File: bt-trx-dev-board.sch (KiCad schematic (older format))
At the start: 13 parts, among them J1 RJ45, J2 PTT_BUTTON, J3 PTT_CON, J5 PTT_SELECT, U1 SILabs_WT32i

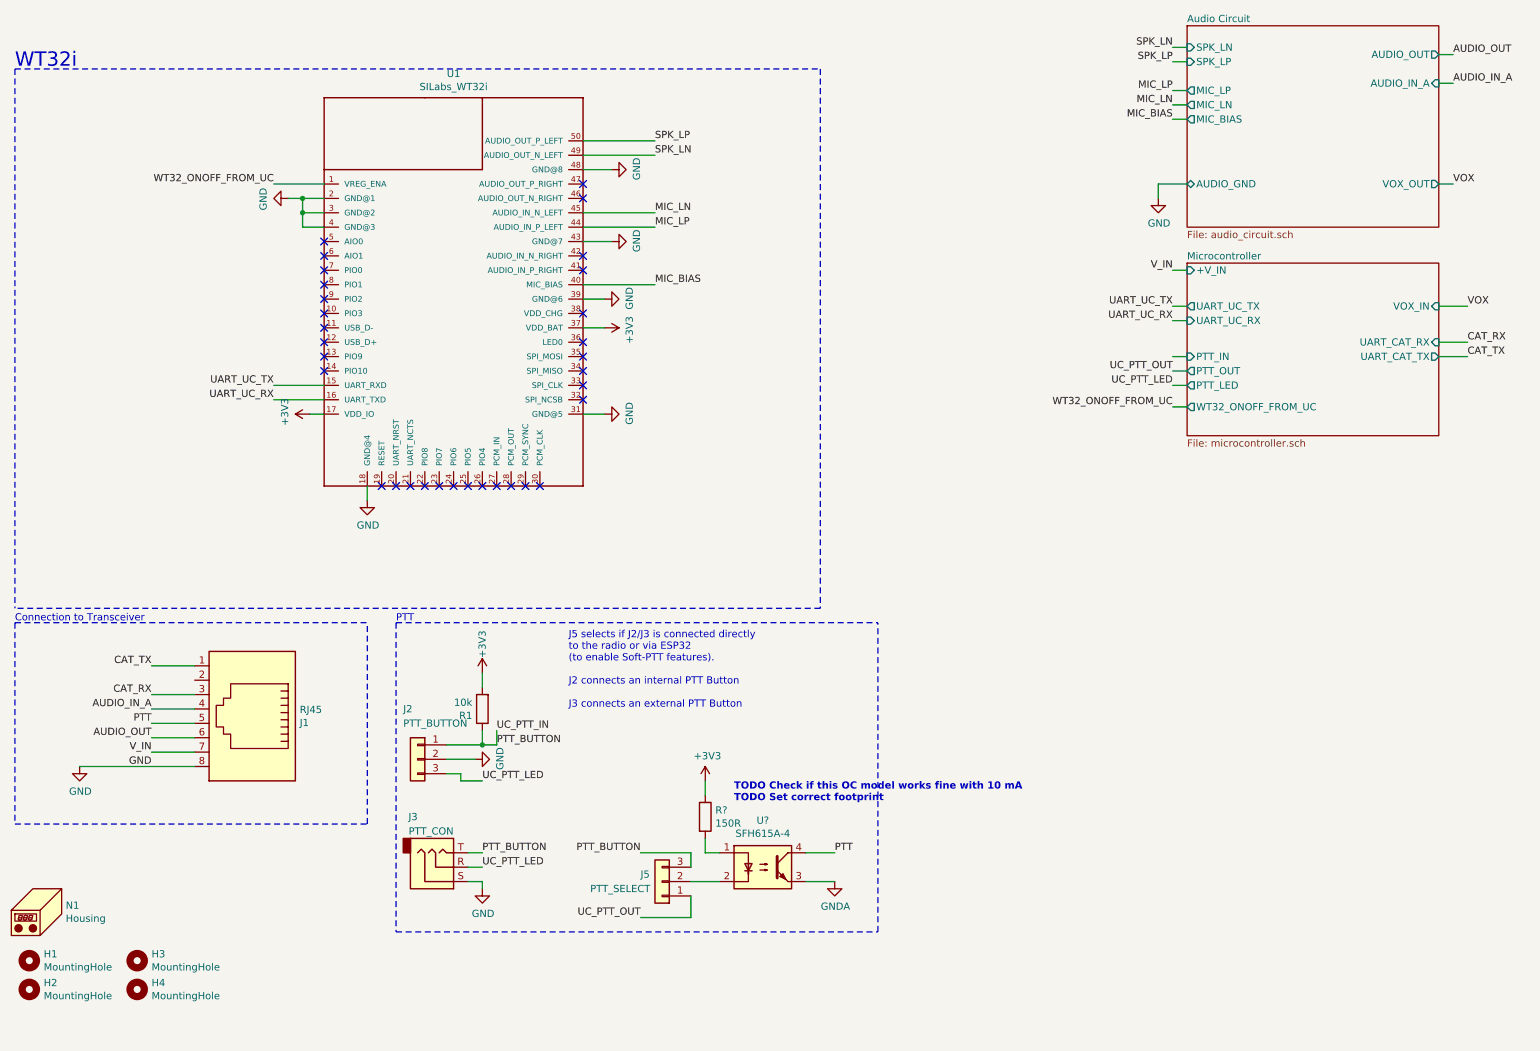
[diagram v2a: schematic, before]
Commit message: Audio Rework in Schematic [#21]
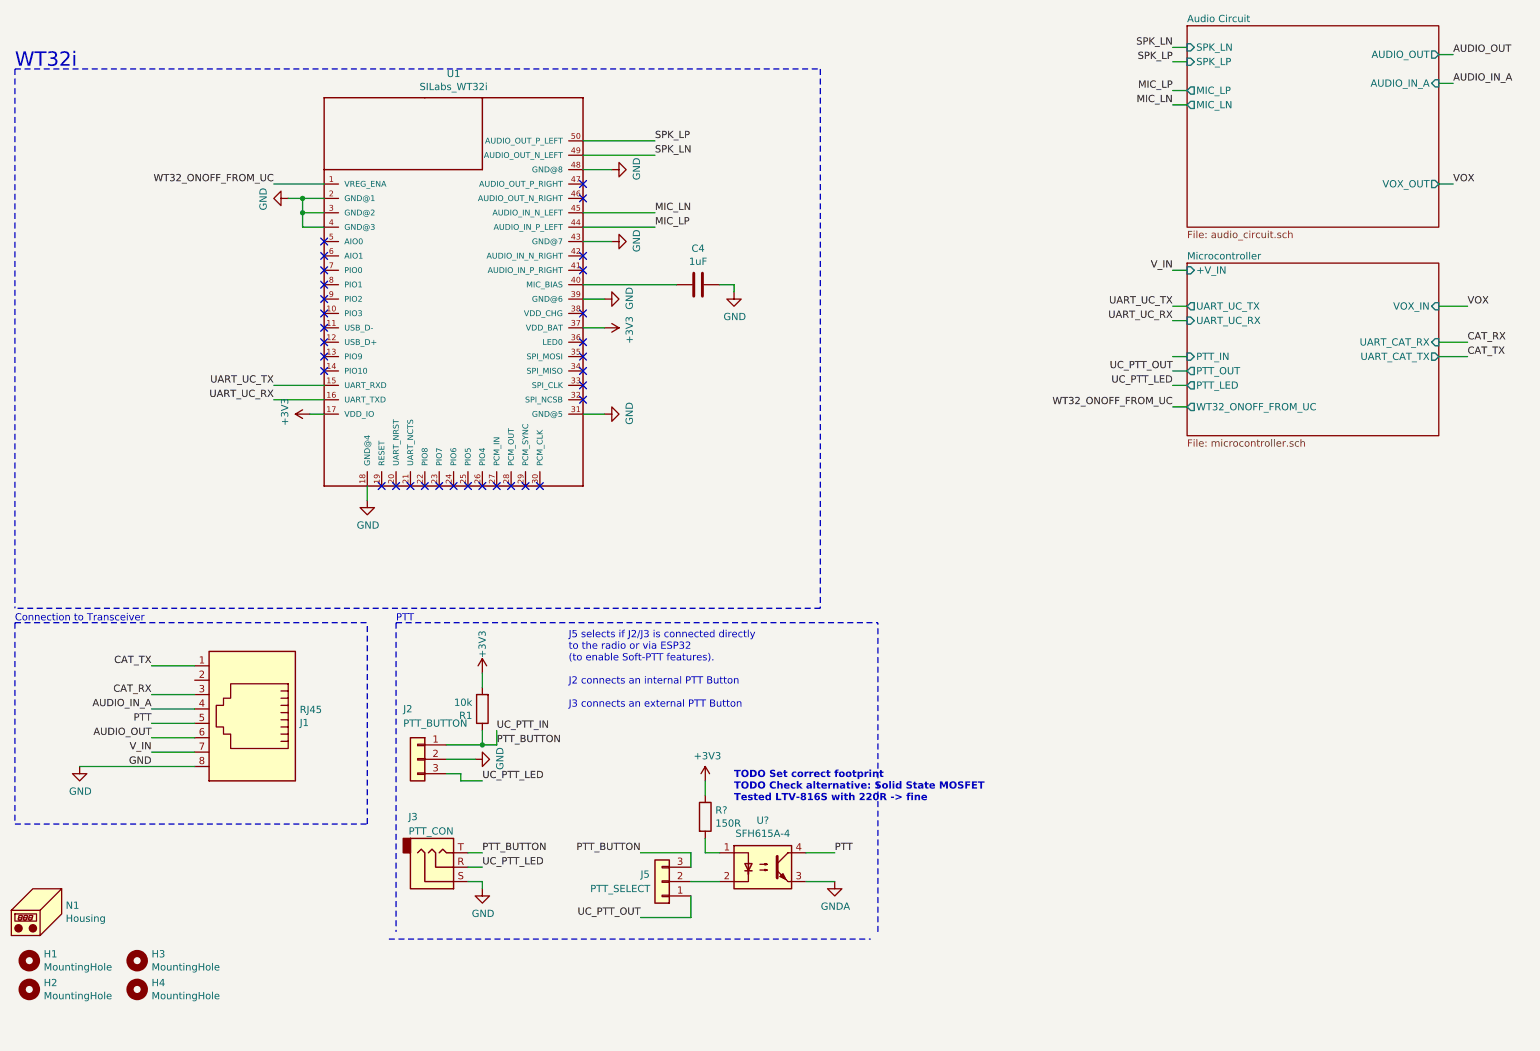
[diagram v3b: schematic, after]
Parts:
- added C4: 1uF, Capacitor_SMD:C_0805_2012Metric_Pad1.15x1.40mm_HandSolder, symbol Device:C
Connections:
- net GND: now also C4.1
- net MIC_BIAS: no longer names the net of U1.40 (MIC_BIAS)
- net MIC_BIAS: now also C4.2
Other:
- note added: "TODO Set correct footprint\nTODO Check alternative: Solid State MOSFET\nTested LTV-816S with 220R -> fine"
- note removed: "TODO Check if this OC model works fine with 10 mA\nTODO Set correct footprint"
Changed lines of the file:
@@
 EESchema Schematic File Version 4
-LIBS:bt-trx-dev-board-cache
 EELAYER 30 0
 EELAYER END
@@
 $EndComp
 NoConn ~ 4650 2650
-Text Label 5150 2450 0    50   ~ 0
-MIC_BIAS
-Wire Wire Line
-	8850 1300 8750 1300
-Text Label 8750 1300 2    50   ~ 0
-MIC_BIAS
 $Comp
 L power:+3V3 #PWR03
@@
 Wire Wire Line
 	4650 2050 5150 2050
-Wire Wire Line
-	4650 2450 5150 2450
 Text Label 2500 3250 2    50   ~ 0
 UART_UC_RX
@@
 F4 "AUDIO_OUT" O R 10600 850 50
 F5 "SPK_LN" I L 8850 800 50
-F6 "MIC_BIAS" O L 8850 1300 50
-F7 "AUDIO_IN_A" I R 10600 1050 50
-F8 "AUDIO_GND" B L 8850 1750 50
-F9 "SPK_LP" I L 8850 900 50
-F10 "VOX_OUT" O R 10600 1750 50
+F6 "AUDIO_IN_A" I R 10600 1050 50
+F7 "SPK_LP" I L 8850 900 50
+F8 "VOX_OUT" O R 10600 1750 50
 $EndSheet
 Wire Wire Line
@@
 Wire Wire Line
 	8850 800  8750 800
-$Comp
-L power:GND #PWR013
-U 1 1 5C781CAB
-P 8650 1850
-F 0 "#PWR013" H 8650 1600 50  0001 C CNN
-F 1 "GND" H 8655 1677 50  0000 C CNN
-F 2 "" H 8650 1850 50  0001 C CNN
-F 3 "" H 8650 1850 50  0001 C CNN
-	1    8650 1850
-	1    0    0    -1
-$EndComp
-Wire Wire Line
-	8850 1750 8650 1750
-Wire Wire Line
-	8650 1750 8650 1850
 $Comp
 L power:GND #PWR010
@@
 	6700 6950 6700 4800
 Wire Notes Line
-	3350 6950 6700 6950
+	3300 7000 6650 7000
 Wire Notes Line
 	3350 4800 6700 4800
@@
 	6200 6600 6400 6600
 Text Notes 5700 6050 0    50   ~ 10
-TODO Check if this OC model works fine with 10 mA\nTODO Set correct footprint
+TODO Set correct footprint\nTODO Check alternative: Solid State MOSFET\nTested LTV-816S with 220R -> fine
 Text Label 4050 5550 0    50   ~ 0
 UC_PTT_IN
@@
 Wire Wire Line
 	4050 5550 4050 5650
+$Comp
+L Device:C C?
+U 1 1 5E304AD9
+P 5450 2450
+AR Path="/5BE3535B/5E304AD9" Ref="C?"  Part="1"
+AR Path="/5E304AD9" Ref="C4"  Part="1"
+F 0 "C4" V 5198 2450 50  0000 C CNN
+F 1 "1uF" V 5289 2450 50  0000 C CNN
+F 2 "Capacitor_SMD:C_0805_2012Metric_Pad1.15x1.40mm_HandSolder" H 5488 2300 50  0001 C CNN
+F 3 "~" H 5450 2450 50  0001 C CNN
+F 4 "80-C0805C105K3RAUTO" H 3700 -4400 50  0001 C CNN "Mouser Best.Nr."
+	1    5450 2450
+	0    1    1    0
+$EndComp
+Wire Wire Line
+	5700 2450 5700 2500
+Wire Wire Line
+	5600 2450 5700 2450
+Wire Wire Line
+	4650 2450 5300 2450
+$Comp
+L power:GND #PWR?
+U 1 1 5E304AE2
+P 5700 2500
+AR Path="/5BE3535B/5E304AE2" Ref="#PWR?"  Part="1"
+AR Path="/5E304AE2" Ref="#PWR?"  Part="1"
+F 0 "#PWR?" H 5700 2250 50  0001 C CNN
+F 1 "GND" H 5705 2327 50  0000 C CNN
+F 2 "" H 5700 2500 50  0001 C CNN
+F 3 "" H 5700 2500 50  0001 C CNN
+	1    5700 2500
+	1    0    0    -1
+$EndComp
 $EndSCHEMATC

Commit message: Further Audio Rework, separation of AGND and MIC_GND [#21]
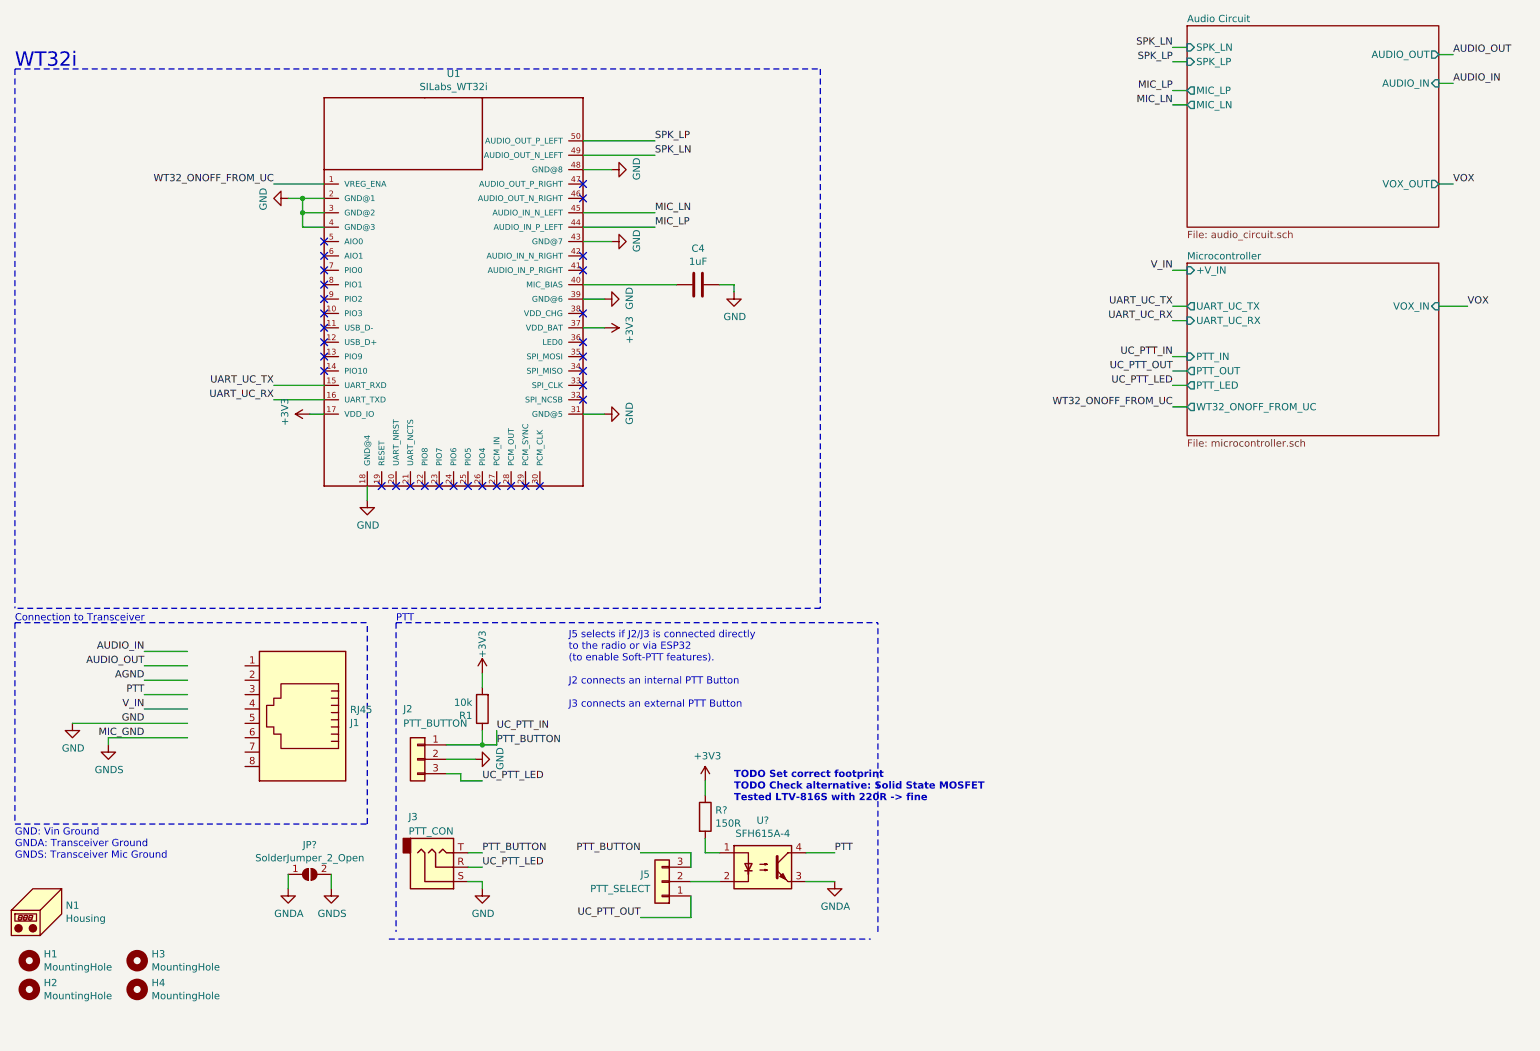
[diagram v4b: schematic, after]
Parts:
- added JP?: SolderJumper_2_Open, symbol Jumper:SolderJumper_2_Open
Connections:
- net labels added: AGND, AUDIO_IN, GNDS, MIC_GND
- net labels removed: AUDIO_IN_A, CAT_RX, CAT_TX
- wire segments 70 -> 71
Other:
- note added: "GND: Vin Ground\nGNDA: Transceiver Ground\nGNDS: Transceiver Mic Ground"
- moved on the sheet: J1
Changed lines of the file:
@@
 Wire Wire Line
 	2500 3250 2850 3250
-Text Label 1650 5400 2    50   ~ 0
-AUDIO_IN_A
-Text Label 1650 5600 2    50   ~ 0
-AUDIO_OUT
 Wire Wire Line
 	10600 850  10700 850
@@
 AUDIO_OUT
 Text Label 10700 1050 0    50   ~ 0
-AUDIO_IN_A
-Text Label 1650 5500 2    50   ~ 0
-PTT
-Wire Wire Line
-	1650 5500 1950 5500
-Wire Wire Line
-	1650 5400 1950 5400
-Wire Wire Line
-	1650 5300 1950 5300
-Text Label 1650 5100 2    50   ~ 0
-CAT_TX
-Text Label 1650 5300 2    50   ~ 0
-CAT_RX
+AUDIO_IN
 Wire Notes Line
 	3150 6200 3150 4800
@@
 Text Notes 700  4800 0    50   ~ 0
 Connection to Transceiver
-Text Label 1650 5700 2    50   ~ 0
-V_IN
-Text Label 1650 5800 2    50   ~ 0
-GND
 Wire Wire Line
 	8850 2350 8750 2350
@@
 F4 "AUDIO_OUT" O R 10600 850 50
 F5 "SPK_LN" I L 8850 800 50
-F6 "AUDIO_IN_A" I R 10600 1050 50
+F6 "AUDIO_IN" I R 10600 1050 50
 F7 "SPK_LP" I L 8850 900 50
 F8 "VOX_OUT" O R 10600 1750 50
@@
 Wire Wire Line
 	5150 1450 4650 1450
-Wire Wire Line
-	10600 2850 10800 2850
-Wire Wire Line
-	10600 2950 10800 2950
-Text Label 10800 2950 0    50   ~ 0
-CAT_TX
-Text Label 10800 2850 0    50   ~ 0
-CAT_RX
 $Comp
 L Connector_Generic:Conn_01x03 J5
@@
 F4 "WT32_ONOFF_FROM_UC" O L 8850 3300 50
 F5 "+V_IN" I L 8850 2350 50
-F6 "UART_CAT_RX" I R 10600 2850 50
-F7 "UART_CAT_TX" O R 10600 2950 50
-F8 "PTT_IN" I L 8850 2950 50
-F9 "PTT_OUT" O L 8850 3050 50
-F10 "PTT_LED" O L 8850 3150 50
-F11 "VOX_IN" I R 10600 2600 50
+F6 "PTT_IN" I L 8850 2950 50
+F7 "PTT_OUT" O L 8850 3050 50
+F8 "PTT_LED" O L 8850 3150 50
+F9 "VOX_IN" I R 10600 2600 50
 $EndSheet
 Wire Wire Line
@@
 Wire Wire Line
 	3850 6600 3950 6600
-$Comp
-L power:GND #PWR01
-U 1 1 5C038459
-P 1150 5800
-F 0 "#PWR01" H 1150 5550 50  0001 C CNN
-F 1 "GND" H 1155 5627 50  0000 C CNN
-F 2 "" H 1150 5800 50  0001 C CNN
-F 3 "" H 1150 5800 50  0001 C CNN
-	1    1150 5800
-	1    0    0    -1
-$EndComp
-Wire Wire Line
-	1950 5700 1650 5700
-Wire Wire Line
-	1650 5100 1950 5100
 Wire Notes Line
 	700  6200 3150 6200
@@
 L Connector:RJ45 J1
 U 1 1 5C7A0AB1
-P 2350 5400
-F 0 "J1" H 2020 5496 50  0000 R CNN
-F 1 "RJ45" H 2020 5405 50  0000 R CNN
-F 2 "Connector_RJ:RJ45_Amphenol_54602-x08_Horizontal" V 2350 5425 50  0001 C CNN
-F 3 "~" V 2350 5425 50  0001 C CNN
-F 4 "649-54602-908LF " H -7250 -350 50  0001 C CNN "Mouser Best.Nr."
-	1    2350 5400
+P 2700 5400
+F 0 "J1" H 2370 5496 50  0000 R CNN
+F 1 "RJ45" H 2370 5405 50  0000 R CNN
+F 2 "Connector_RJ:RJ45_Amphenol_54602-x08_Horizontal" V 2700 5425 50  0001 C CNN
+F 3 "~" V 2700 5425 50  0001 C CNN
+F 4 "649-54602-908LF " H -6900 -350 50  0001 C CNN "Mouser Best.Nr."
+	1    2700 5400
 	-1   0    0    1
 $EndComp
-Wire Wire Line
-	1950 5600 1650 5600
-Wire Wire Line
-	1150 5800 1950 5800
 $Comp
 L Mechanical:Housing N1
@@
 	1    0    0    -1
 $EndComp
+Wire Wire Line
+	1900 5300 1600 5300
+Text Label 1600 5300 2    50   ~ 0
+PTT
+Wire Wire Line
+	1600 5000 1900 5000
+Text Label 1600 5000 2    50   ~ 0
+AUDIO_IN
+Text Label 1600 5200 2    50   ~ 0
+AGND
+Wire Wire Line
+	1600 5200 1900 5200
+Wire Wire Line
+	1600 5100 1900 5100
+Text Label 1600 5100 2    50   ~ 0
+AUDIO_OUT
+Wire Wire Line
+	1100 5500 1900 5500
+$Comp
+L power:GND #PWR01
+U 1 1 5C038459
+P 1100 5500
+F 0 "#PWR01" H 1100 5250 50  0001 C CNN
+F 1 "GND" H 1105 5327 50  0000 C CNN
+F 2 "" H 1100 5500 50  0001 C CNN
+F 3 "" H 1100 5500 50  0001 C CNN
+	1    1100 5500
+	1    0    0    -1
+$EndComp
+Text Label 1600 5500 2    50   ~ 0
+GND
+Text Label 1600 5400 2    50   ~ 0
+V_IN
+Wire Wire Line
+	1600 5400 1900 5400
+$Comp
+L power:GNDS #PWR?
+U 1 1 5E43D183
+P 1350 5650
+F 0 "#PWR?" H 1350 5400 50  0001 C CNN
+F 1 "GNDS" H 1355 5477 50  0000 C CNN
+F 2 "" H 1350 5650 50  0001 C CNN
+F 3 "" H 1350 5650 50  0001 C CNN
+	1    1350 5650
+	1    0    0    -1
+$EndComp
+Wire Wire Line
+	1350 5650 1350 5600
+Wire Wire Line
+	1350 5600 1900 5600
+Text Label 1600 5600 2    50   ~ 0
+MIC_GND
+$Comp
+L power:GNDS #PWR?
+U 1 1 5E442634
+P 2900 6650
+F 0 "#PWR?" H 2900 6400 50  0001 C CNN
+F 1 "GNDS" H 2905 6477 50  0000 C CNN
+F 2 "" H 2900 6650 50  0001 C CNN
+F 3 "" H 2900 6650 50  0001 C CNN
+	1    2900 6650
+	1    0    0    -1
+$EndComp
+$Comp
+L power:GNDA #PWR?
+U 1 1 5E4433A4
+P 2600 6650
+F 0 "#PWR?" H 2600 6400 50  0001 C CNN
+F 1 "GNDA" H 2605 6477 50  0000 C CNN
+F 2 "" H 2600 6650 50  0001 C CNN
+F 3 "" H 2600 6650 50  0001 C CNN
+	1    2600 6650
+	1    0    0    -1
+$EndComp
+$Comp
+L Jumper:SolderJumper_2_Open JP?
+U 1 1 5E445652
+P 2750 6550
+F 0 "JP?" H 2750 6755 50  0000 C CNN
+F 1 "SolderJumper_2_Open" H 2750 6664 50  0000 C CNN
+F 2 "" H 2750 6550 50  0001 C CNN
+F 3 "~" H 2750 6550 50  0001 C CNN
+	1    2750 6550
+	1    0    0    -1
+$EndComp
+Wire Wire Line
+	2600 6650 2600 6550
+Wire Wire Line
+	2900 6550 2900 6650
+Text Notes 700  6450 0    50   ~ 0
+GND: Vin Ground\nGNDA: Transceiver Ground\nGNDS: Transceiver Mic Ground
+Text Label 8750 2950 2    50   ~ 0
+UC_PTT_IN
 $EndSCHEMATC
